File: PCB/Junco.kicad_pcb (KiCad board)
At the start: 2 copper layers, 296.6 x 130.5 mm, 205 parts, among them J1 AudioJack4, J2 AudioJack4, SW1 SW_Push, SW10 SW_Push, SW11 SW_Push, SW12 SW_Push, SW13 SW_Push, SW14 SW_Push, SW15 SW_Push, SW16 SW_Push, SW17 SW_Push, SW18 SW_Push, SW19 SW_MX_Hotswap_Rotary, SW2 SW_Push, SW20 SW_Push, SW21 SW_Push, SW22 SW_Push, SW23 SW_Push, SW24 SW_Push, SW25 SW_Push, SW26 SW_Push, SW27 SW_Push, SW28 SW_Push, SW29 SW_Push, SW3 SW_Push, SW30 RotaryEncoder_Switch, SW31 SW_Push, SW32 SW_Push, SW33 SW_Push, SW34 SW_Push, SW35 SW_Push, SW36 SW_Push, SW37 SW_Push, SW38 SW_Push, SW39 SW_Push, SW4 SW_Push, SW40 SW_Push, SW41 SW_Push, SW42 SW_Push, SW43 SW_Push, SW44 SW_Push, SW45 SW_Push, SW46 SW_Push, SW47 SW_Push, SW48 SW_Push, SW49 SW_MX_Hotswap_Rotary, SW5 SW_Push, SW50 SW_Push, SW51 SW_Push, SW52 SW_Push, SW53 SW_Push, SW54 SW_Push, SW55 SW_Push, SW56 SW_Push, SW57 SW_Push, SW58 SW_Push, SW59 SW_Push, SW6 SW_Push, SW60 RotaryEncoder_Switch, SW7 SW_Push, SW8 SW_Push, SW9 SW_Push, U1 Pico, U2 SN74AHCT1G125, U3 Pico, U4 SN74AHCT1G125

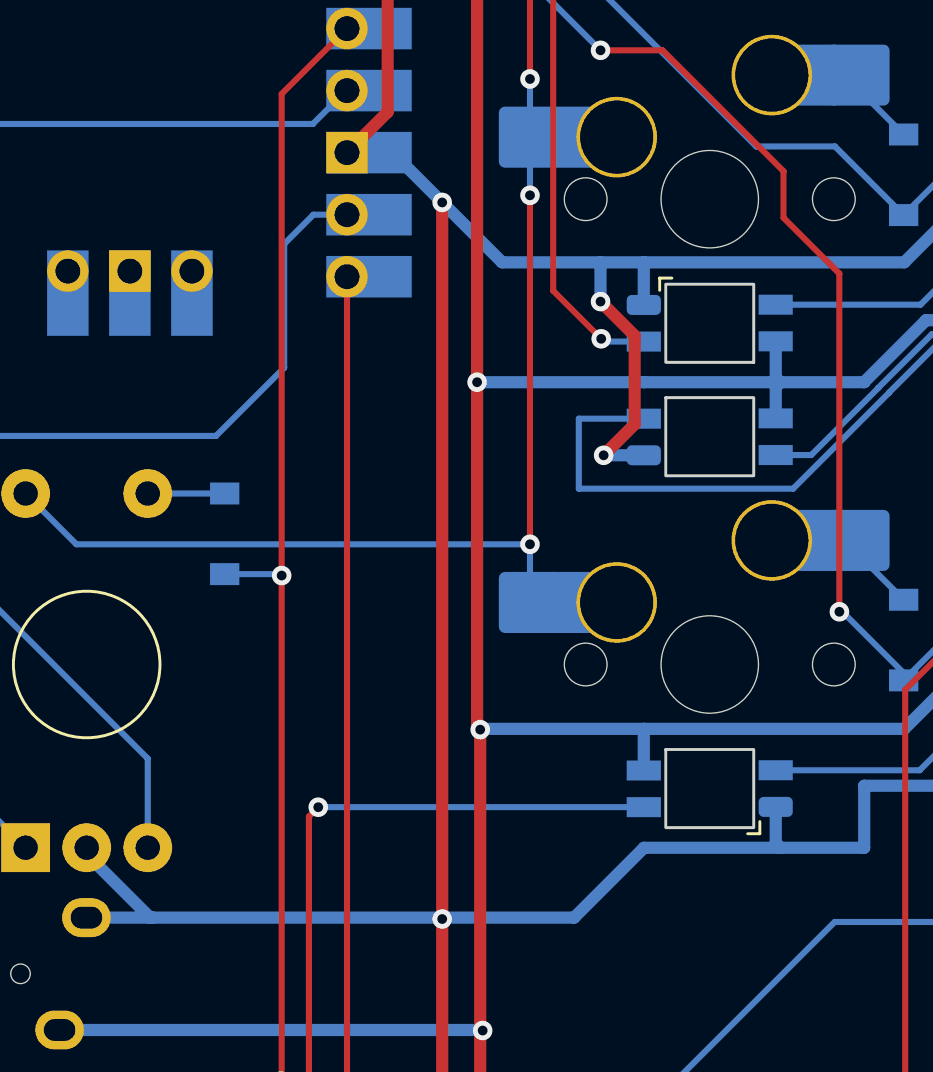
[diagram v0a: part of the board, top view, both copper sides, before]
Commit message: Clean up some traces
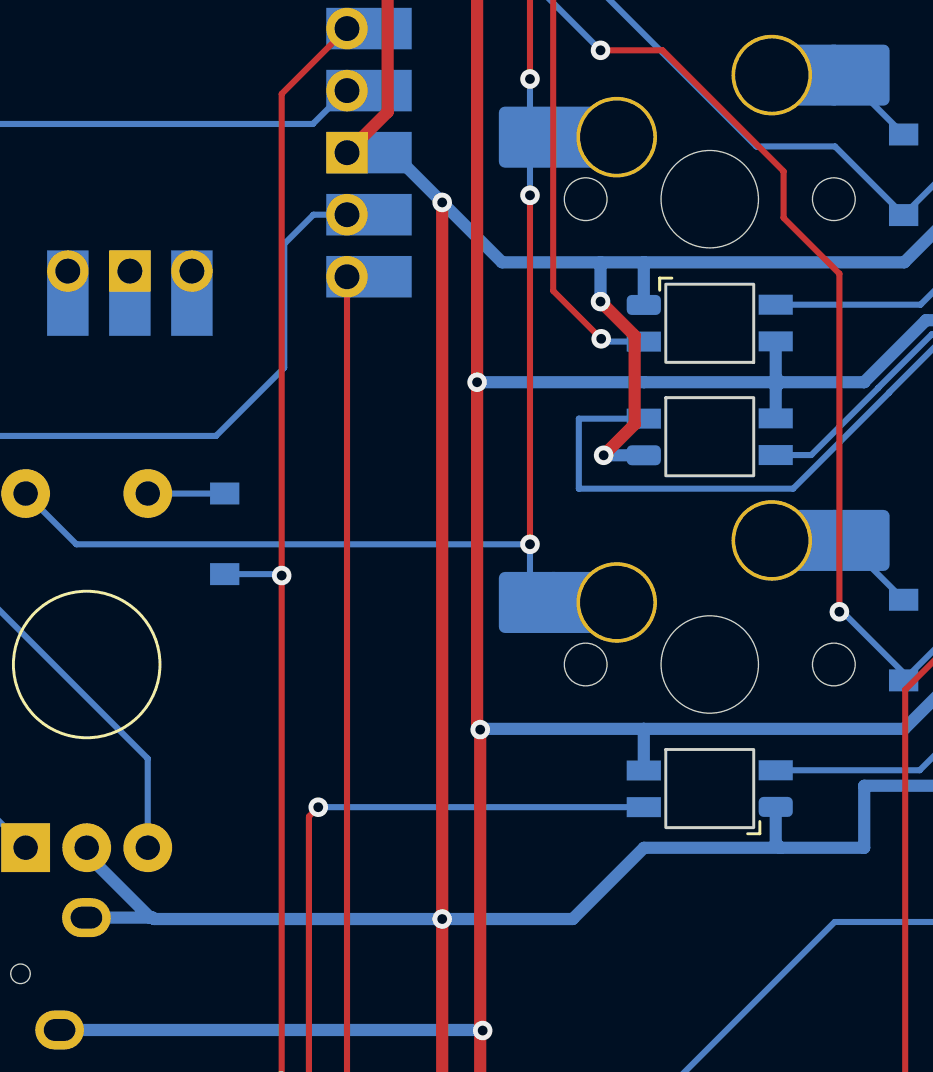
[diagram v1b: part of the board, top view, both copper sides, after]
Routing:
- net GNDA: track 892.9 -> 894.9 mm
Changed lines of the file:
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@@
   (net 215 "unconnected-(U1-Pad38)")
   (net 216 "unconnected-(U3-Pad3)")
-  (net 217 "Net-(U1-Pad40)")
-  (net 218 "Net-(U3-Pad40)")
+  (net 217 "Net-(D61-Pad2)")
+  (net 218 "Net-(D62-Pad2)")
   (footprint "Junco:D_SOD-123" (layer "F.Cu")
     (at 258.8247 56.15)
@@
       (net 64 "VCC") (pinfunction "K") (pintype "passive"))
     (pad "2" smd rect (at 0 -1.65 270) (size 0.9 1.2) (layers "B.Cu" "B.Paste" "B.Mask")
-      (net 217 "Net-(U1-Pad40)") (pinfunction "A") (pintype "passive"))
+      (net 217 "Net-(D61-Pad2)") (pinfunction "A") (pintype "passive"))
     (model "${KICAD6_3DMODEL_DIR}/Diode_SMD.3dshapes/D_SOD-123.wrl"
       (offset (xyz 0 0 -1.6))
@@
       (net 86 "VDD") (pinfunction "K") (pintype "passive"))
     (pad "2" smd rect (at 0 -1.65 270) (size 0.9 1.2) (layers "B.Cu" "B.Paste" "B.Mask")
-      (net 218 "Net-(U3-Pad40)") (pinfunction "A") (pintype "passive"))
+      (net 218 "Net-(D62-Pad2)") (pinfunction "A") (pintype "passive"))
     (model "${KICAD6_3DMODEL_DIR}/Diode_SMD.3dshapes/D_SOD-123.wrl"
       (offset (xyz 0 0 -1.6))
@@
     (fp_line (start 8.685176 3.75022) (end 8.685176 1.30022) (layer "B.CrtYd") (width 0.05))
     (fp_arc (start 6.085176 4.75022) (mid 5.499388 6.164433) (end 4.085176 6.75022) (layer "B.CrtYd") (width 0.05))
-    (fp_arc (start 2.494322 0.86022) (mid 1.670504 2.183399) (end 0.2 2.70022) (layer "B.CrtYd") (width 0.05))
+    (fp_arc (start 2.494322 0.86022) (mid 1.670503 2.1834) (end 0.2 2.70022) (layer "B.CrtYd") (width 0.05))
     (fp_line (start -7 7) (end 7 7) (layer "F.CrtYd") (width 0.05))
     (fp_line (start 7 -7) (end -7 -7) (layer "F.CrtYd") (width 0.05))
@@
     (fp_line (start 6.085176 0.86022) (end 2.494322 0.86022) (layer "B.CrtYd") (width 0.05))
     (fp_arc (start 6.085176 4.75022) (mid 5.499388 6.164433) (end 4.085176 6.75022) (layer "B.CrtYd") (width 0.05))
-    (fp_arc (start 2.494322 0.86022) (mid 1.670504 2.183399) (end 0.2 2.70022) (layer "B.CrtYd") (width 0.05))
+    (fp_arc (start 2.494322 0.86022) (mid 1.670503 2.1834) (end 0.2 2.70022) (layer "B.CrtYd") (width 0.05))
     (fp_line (start 7 -7) (end -7 -7) (layer "F.CrtYd") (width 0.05))
     (fp_line (start -7 -7) (end -7 7) (layer "F.CrtYd") (width 0.05))
@@
       (net 86 "VDD") (pinfunction "VSYS") (pintype "power_in"))
     (pad "40" thru_hole oval (at 8.89 24.13 180) (size 1.7 1.7) (drill 1.02) (layers *.Cu *.Mask)
-      (net 218 "Net-(U3-Pad40)") (pinfunction "VBUS") (pintype "power_in"))
+      (net 218 "Net-(D62-Pad2)") (pinfunction "VBUS") (pintype "power_in"))
     (pad "40" smd rect (at 8.89 24.13 180) (size 3.5 1.7) (drill (offset 0.9 0)) (layers "B.Cu" "B.Mask")
-      (net 218 "Net-(U3-Pad40)") (pinfunction "VBUS") (pintype "power_in"))
+      (net 218 "Net-(D62-Pad2)") (pinfunction "VBUS") (pintype "power_in"))
     (pad "41" thru_hole oval (at -2.54 -23.9 180) (size 1.7 1.7) (drill 1.02) (layers *.Cu *.Mask)
       (net 137 "unconnected-(U3-Pad41)") (pinfunction "SWCLK") (pintype "input+no_connect"))
@@
       (net 64 "VCC") (pinfunction "VSYS") (pintype "power_in"))
     (pad "40" smd rect (at 8.89 24.13 180) (size 3.5 1.7) (drill (offset 0.9 0)) (layers "B.Cu" "B.Mask")
-      (net 217 "Net-(U1-Pad40)") (pinfunction "VBUS") (pintype "power_in"))
+      (net 217 "Net-(D61-Pad2)") (pinfunction "VBUS") (pintype "power_in"))
     (pad "40" thru_hole oval (at 8.89 24.13 180) (size 1.7 1.7) (drill 1.02) (layers *.Cu *.Mask)
-      (net 217 "Net-(U1-Pad40)") (pinfunction "VBUS") (pintype "power_in"))
+      (net 217 "Net-(D61-Pad2)") (pinfunction "VBUS") (pintype "power_in"))
     (pad "41" thru_hole oval (at -2.54 -23.9 180) (size 1.7 1.7) (drill 1.02) (layers *.Cu *.Mask)
       (net 119 "unconnected-(U1-Pad41)") (pinfunction "SWCLK") (pintype "input+no_connect"))
@@
   (segment (start 253.5872 123.275) (end 253.5872 121.76) (width 0.5) (layer "B.Cu") (net 86))
   (segment (start 266.6085 50.927) (end 272.9585 50.927) (width 0.5) (layer "B.Cu") (net 86))
+  (segment (start 201.833161 127.756661) (end 201.833161 113.670339) (width 0.5) (layer "F.Cu") (net 87))
   (segment (start 245.6535 118.745) (end 245.6535 124.206) (width 0.5) (layer "F.Cu") (net 87))
-  (segment (start 201.8385 127.762) (end 201.833161 127.756661) (width 0.5) (layer "F.Cu") (net 87))
   (segment (start 256.3215 42.291) (end 256.3215 46.863) (width 0.5) (layer "F.Cu") (net 87))
   (segment (start 209.7125 93.415) (end 208.4425 94.685) (width 0.5) (layer "F.Cu") (net 87))
   (segment (start 218.4755 49.911) (end 218.4755 54.991) (width 0.5) (layer "F.Cu") (net 87))
+  (segment (start 201.8385 127.762) (end 201.833161 127.756661) (width 0.5) (layer "F.Cu") (net 87))
   (segment (start 294.1942 97.409) (end 294.1942 104.14) (width 0.5) (layer "F.Cu") (net 87))
   (segment (start 197.9358 69.595) (end 196.1716 67.8308) (width 0.5) (layer "F.Cu") (net 87))
@@
   (segment (start 197.9358 82.295) (end 199.6006 80.6302) (width 0.5) (layer "F.Cu") (net 87))
   (segment (start 201.833161 84.333339) (end 201.833161 113.670339) (width 0.5) (layer "F.Cu") (net 87))
-  (segment (start 201.833161 127.756661) (end 201.833161 113.670339) (width 0.5) (layer "F.Cu") (net 87))
   (segment (start 208.3155 88.392) (end 209.7125 89.789) (width 0.5) (layer "F.Cu") (net 87))
   (segment (start 196.1716 67.8308) (end 196.1716 58.6592) (width 0.5) (layer "F.Cu") (net 87))
@@
   (segment (start 196.42508 127.234923) (end 196.42508 125.80942) (width 0.5) (layer "B.Cu") (net 87))
   (segment (start 245.364221 116.873421) (end 248.186779 116.873421) (width 0.5) (layer "B.Cu") (net 87))
+  (segment (start 201.833161 113.670339) (end 190.035999 113.670339) (width 0.5) (layer "B.Cu") (net 87))
   (segment (start 196.42508 125.80942) (end 196.5045 125.73) (width 0.5) (layer "B.Cu") (net 87))
   (segment (start 303.4385 120.152) (end 303.4385 121.793) (width 0.5) (layer "B.Cu") (net 87))
@@
   (segment (start 266.6185 108.087) (end 261.2845 102.753) (width 0.5) (layer "B.Cu") (net 87))
   (segment (start 308.1375 122.555) (end 312.3285 122.555) (width 0.5) (layer "B.Cu") (net 87))
+  (segment (start 201.833161 113.670339) (end 207.177161 113.670339) (width 0.5) (layer "B.Cu") (net 87))
   (segment (start 220.7522 48.685) (end 223.2772 46.16) (width 0.5) (layer "B.Cu") (net 87))
   (segment (start 248.1872 118.63) (end 248.1872 116.873842) (width 0.5) (layer "B.Cu") (net 87))
@@
   (segment (start 291.6872 120.0823) (end 291.6175 120.152) (width 0.5) (layer "B.Cu") (net 87))
   (segment (start 253.5872 62.98) (end 253.5872 64.3317) (width 0.5) (layer "B.Cu") (net 87))
-  (segment (start 215.6815 110.754) (end 210.0935 110.754) (width 0.5) (layer "B.Cu") (net 87))
   (segment (start 219.1105 70.114) (end 219.1105 72.654) (width 0.5) (layer "B.Cu") (net 87))
   (segment (start 234.6045 108.214) (end 219.1105 108.214) (width 0.5) (layer "B.Cu") (net 87))
-  (segment (start 189.97893 113.61327) (end 207.23423 113.61327) (width 0.5) (layer "B.Cu") (net 87))
   (segment (start 194.2452 146.176) (end 193.4852 146.176) (width 0.5) (layer "B.Cu") (net 87))
   (segment (start 207.8442 72.654) (end 215.6815 72.654) (width 0.5) (layer "B.Cu") (net 87))
   (segment (start 201.833161 84.333339) (end 204.284822 86.785) (width 0.5) (layer "B.Cu") (net 87))
+  (segment (start 189.97893 113.61327) (end 190.035999 113.670339) (width 0.5) (layer "B.Cu") (net 87))
   (segment (start 208.9505 130.81) (end 208.9505 128.651) (width 0.5) (layer "B.Cu") (net 87))
   (segment (start 210.0872 50.43) (end 210.0872 48.685) (width 0.5) (layer "B.Cu") (net 87))
@@
   (segment (start 187.2786 111.0164) (end 189.87547 113.61327) (width 0.5) (layer "B.Cu") (net 87))
   (segment (start 312.3285 118.618) (end 312.3285 122.555) (width 0.5) (layer "B.Cu") (net 87))
+  (segment (start 207.177161 113.670339) (end 210.0935 110.754) (width 0.5) (layer "B.Cu") (net 87))
   (segment (start 215.4872 55.0525) (end 218.414 55.0525) (width 0.5) (layer "B.Cu") (net 87))
   (segment (start 253.9085 102.753) (end 242.0975 102.753) (width 0.5) (layer "B.Cu") (net 87))
+  (segment (start 210.0935 110.754) (end 215.6815 110.754) (width 0.5) (layer "B.Cu") (net 87))
   (segment (start 218.5195 48.685) (end 218.5195 49.867) (width 0.5) (layer "B.Cu") (net 87))
   (segment (start 207.1725 132.588) (end 208.9505 130.81) (width 0.5) (layer "B.Cu") (net 87))
@@
   (segment (start 267.2372 84.3447) (end 267.2025 84.31) (width 0.5) (layer "B.Cu") (net 87))
   (segment (start 279.4772 52.236485) (end 279.4772 54.98) (width 0.5) (layer "B.Cu") (net 87))
-  (segment (start 207.23423 113.61327) (end 210.0935 110.754) (width 0.5) (layer "B.Cu") (net 87))
   (segment (start 253.9085 64.653) (end 242.0975 64.653) (width 0.5) (layer "B.Cu") (net 87))
   (segment (start 196.5045 125.73) (end 199.8065 125.73) (width 0.5) (layer "B.Cu") (net 87))
@@
   (segment (start 285.092006 120.152) (end 291.6175 120.152) (width 0.5) (layer "B.Cu") (net 87))
   (segment (start 193.3562 147.193) (end 193.3562 146.176) (width 0.5) (layer "B.Cu") (net 87))
+  (segment (start 199.794822 82.295) (end 197.9358 82.295) (width 0.5) (layer "B.Cu") (net 87))
   (segment (start 278.23798 75.197974) (end 278.23798 71.997265) (width 0.5) (layer "B.Cu") (net 87))
   (segment (start 236.6365 108.214) (end 234.6045 108.214) (width 0.5) (layer "B.Cu") (net 87))
